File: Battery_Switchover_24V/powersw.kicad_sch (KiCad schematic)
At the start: 19 parts, among them Q2 NMOS, Q3 NMOS, Q4 NMOS, Q5 NMOS, Q6 NMOS, Q7 NMOS, U2 LM74610QDGKRQ1

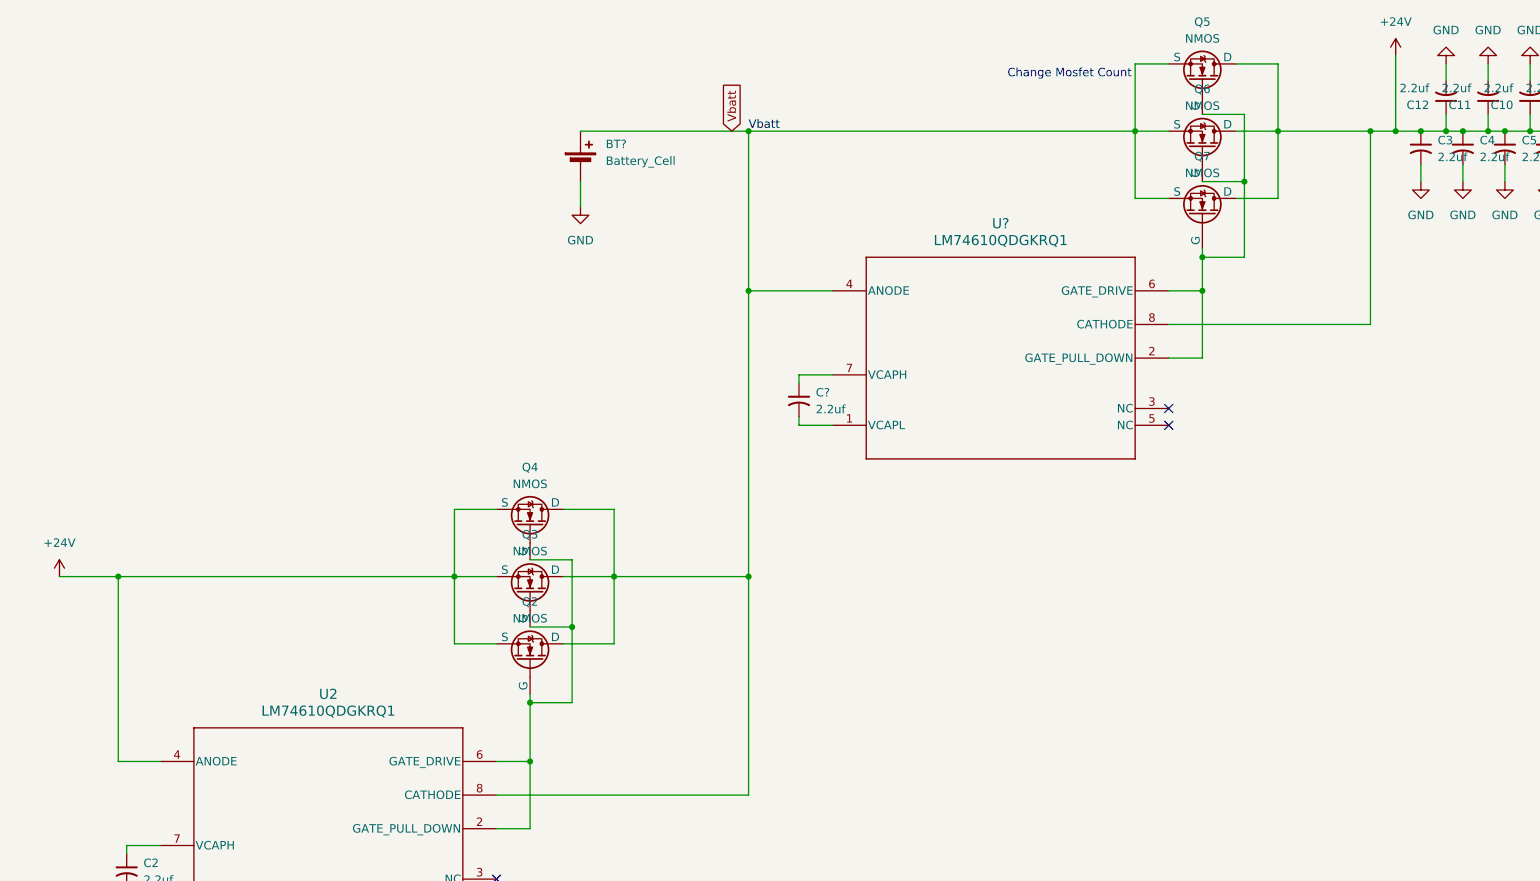
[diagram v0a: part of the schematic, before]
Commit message: General Improvements
Mosfet sayısı 1 e düştü polarize cap ler değiştirildi voltage converter değiştirildi
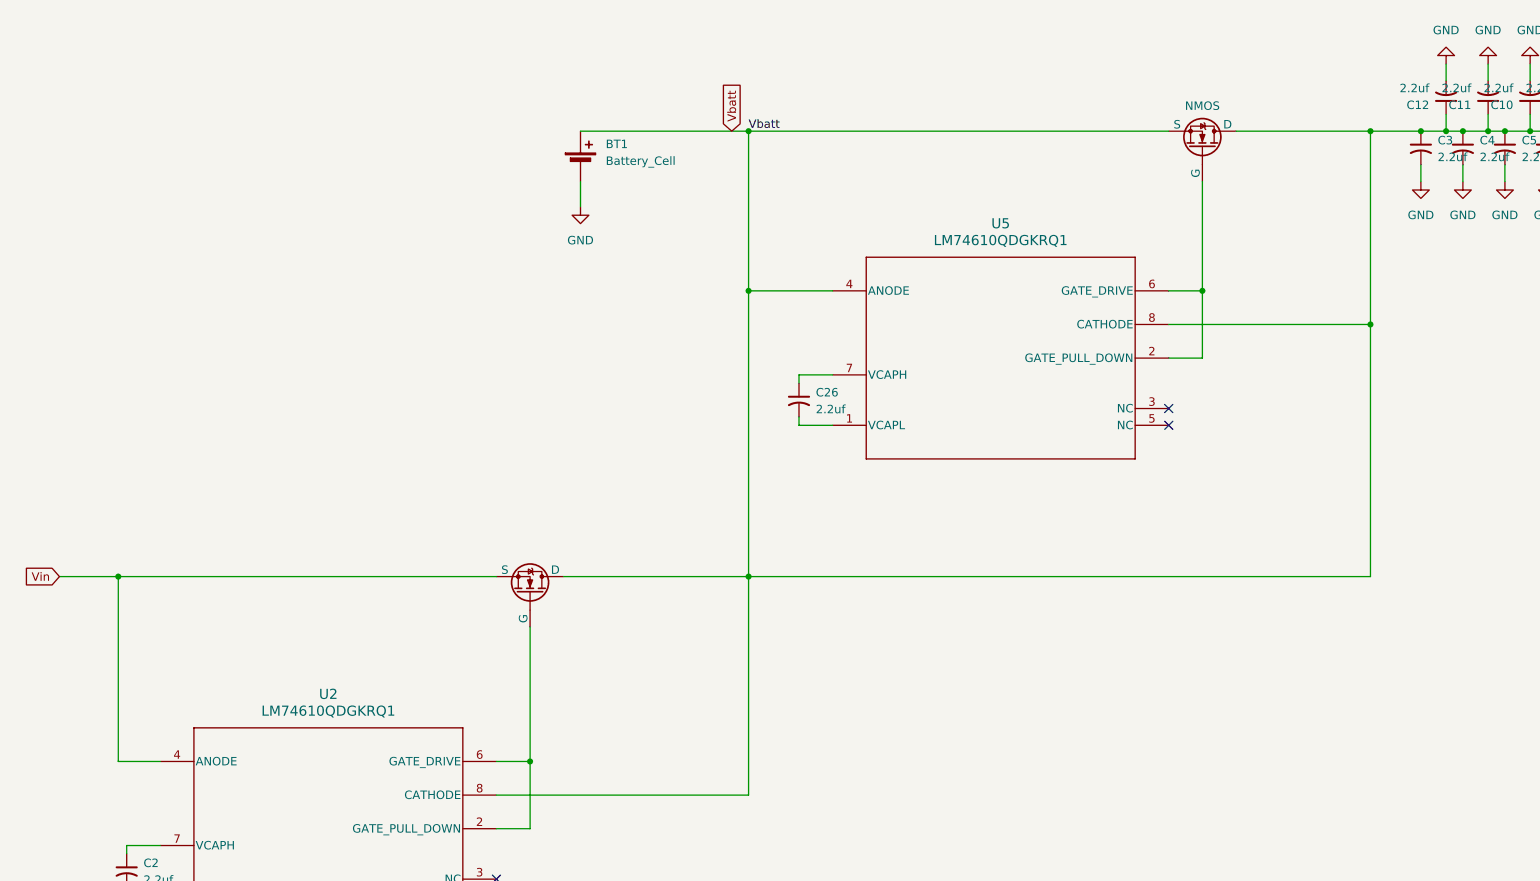
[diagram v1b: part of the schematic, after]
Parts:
- removed Q2, Q4, Q5, Q7: NMOS, symbol Simulation_SPICE:NMOS
- gave numbers to parts that had none: 3
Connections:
- net Vbatt: now also C10.1, C11.1, C12.1, C3.1, C4.1, C5.1, C6.1, C9.1, Q6.1 (D), U5.8 (CATHODE)
- removed net +24V: C10.1, C11.1, C12.1, C3.1, C4.1, C5.1, C6.1, C9.1, Q3.3 (S), Q6.1 (D), U2.4 (ANODE), U5.8 (CATHODE)
- new net Vin: Q3.3 (S), U2.4 (ANODE)
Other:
- note removed: "Change Mosfet Count"

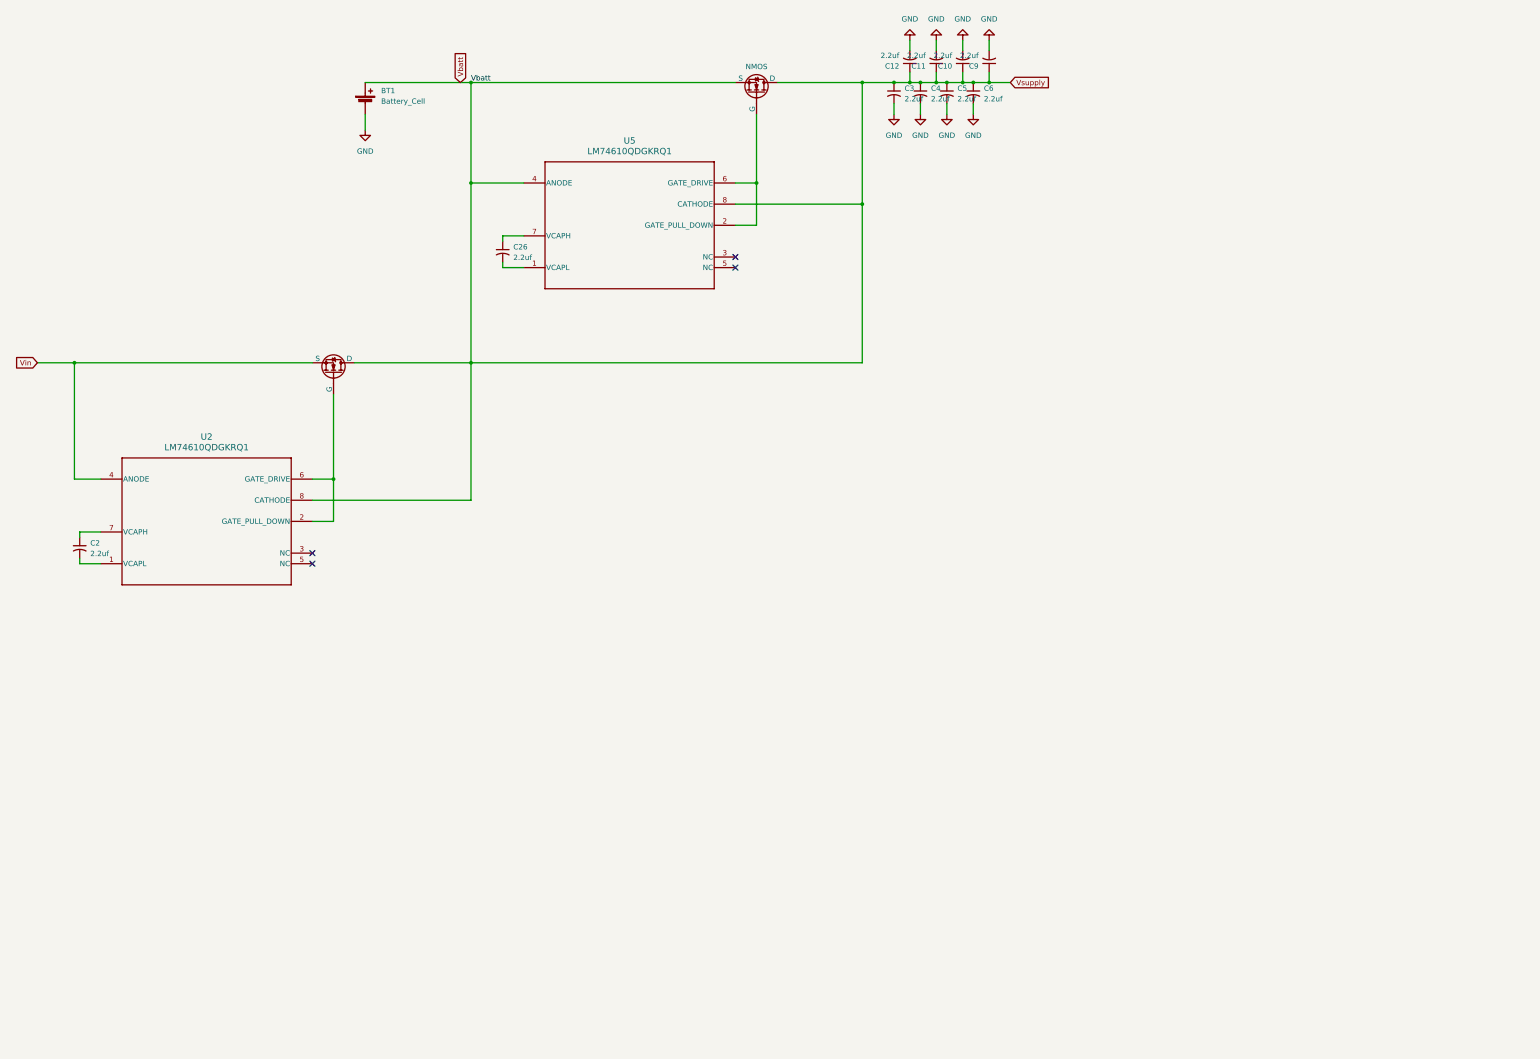
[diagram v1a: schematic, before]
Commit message: Isı kontrollü eklendi bazı parçaların sembolleri değişti
Mosfetlere doğru semboller eklendi Isı kontorll IC eklendi Ledlerin bağlantıları yapıldı
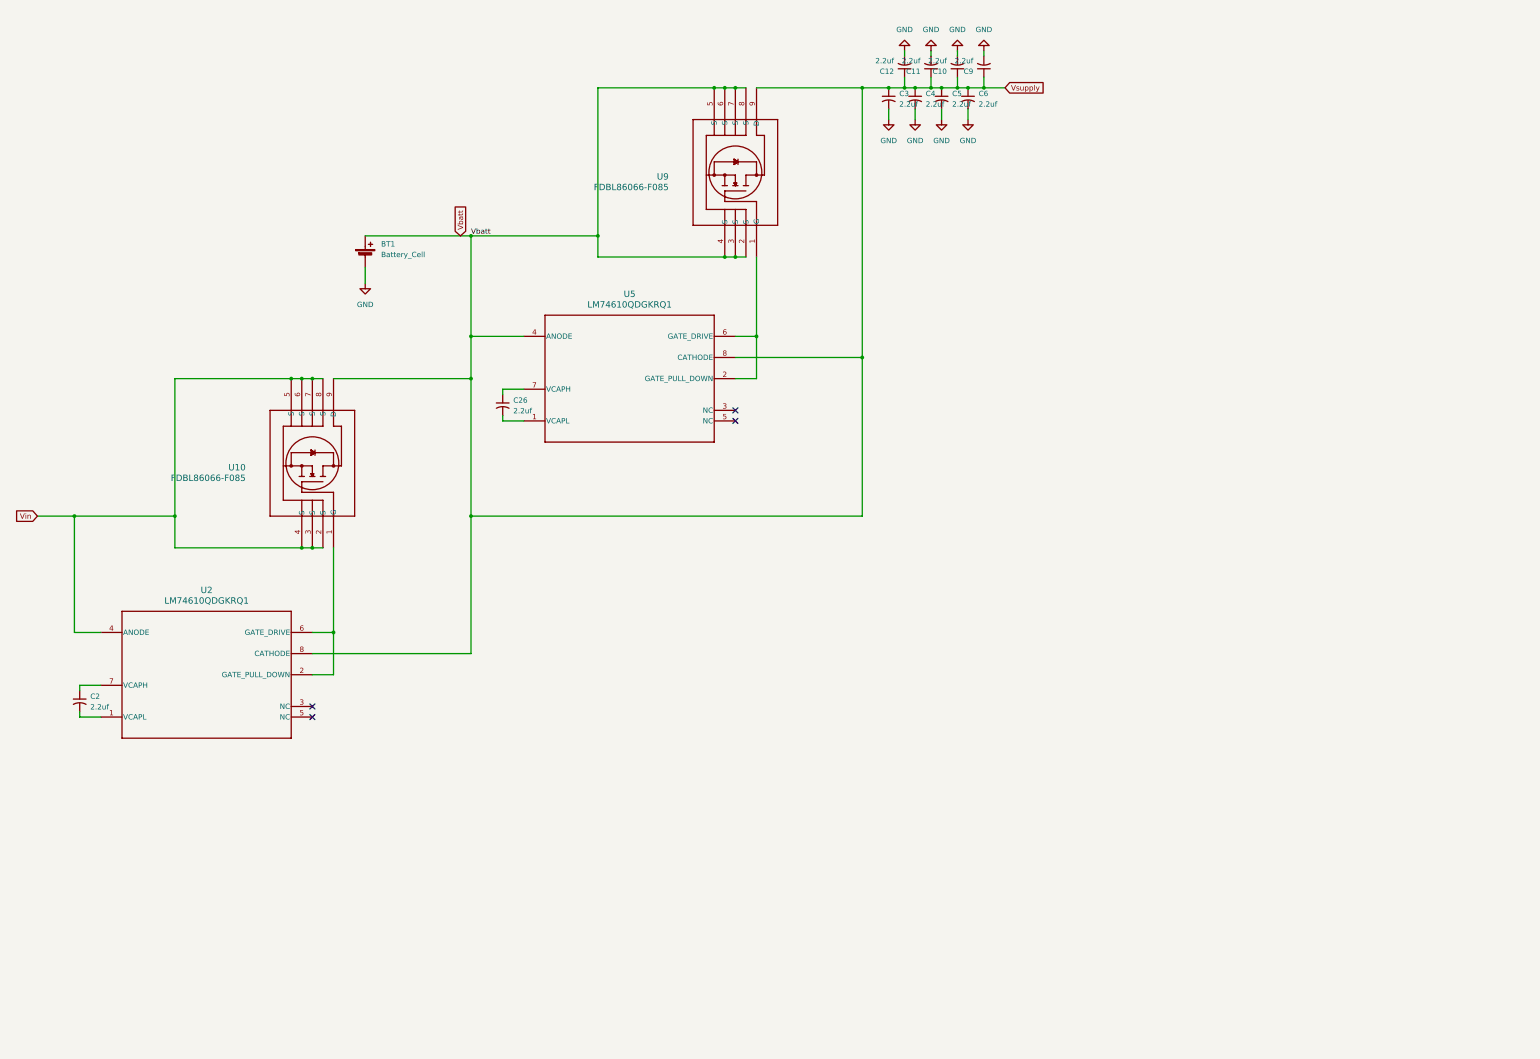
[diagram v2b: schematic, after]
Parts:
- removed Q3, Q6: NMOS, symbol Simulation_SPICE:NMOS
- added U10, U9: FDBL86066-F085, H-PSOF8L_ONS, symbol FDBL86062:FDBL86066-F085
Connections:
- net Vbatt: now also U10.9 (D), U9.2 (S), U9.3 (S), U9.4 (S), U9.5 (S), U9.6 (S), U9.7 (S), U9.8 (S), U9.9 (D)
- net Vin: now also U10.2 (S), U10.3 (S), U10.4 (S), U10.5 (S), U10.6 (S), U10.7 (S), U10.8 (S)
- net at U5.2 (GATE_PULL_DOWN), U5.6 (GATE_DRIVE): now also U9.1 (G)
- net at U2.2 (GATE_PULL_DOWN), U2.6 (GATE_DRIVE): now also U10.1 (G)
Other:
- moved on the sheet: BT1, C10, C11, C12, C2, C26, C3, C4, C5, C6, C9, U2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

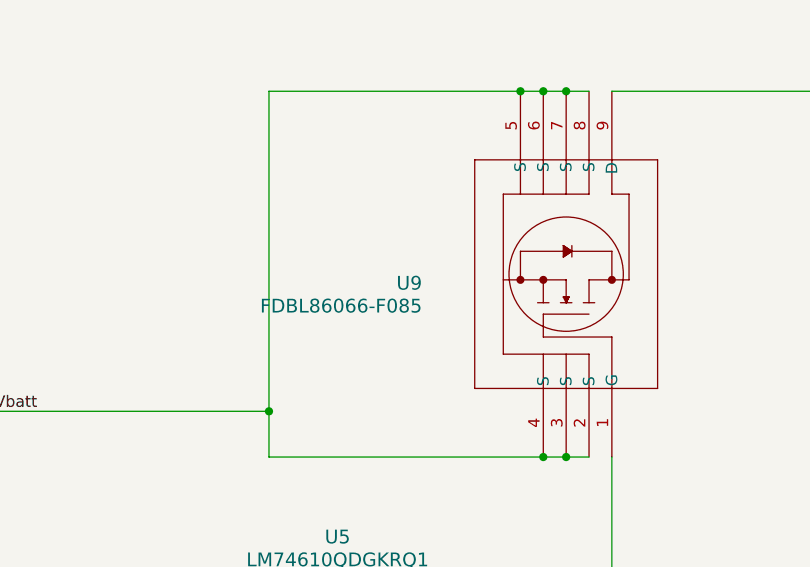
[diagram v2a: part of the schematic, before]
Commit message: Added SCL and SDA from the tempreture sensor to the CPU
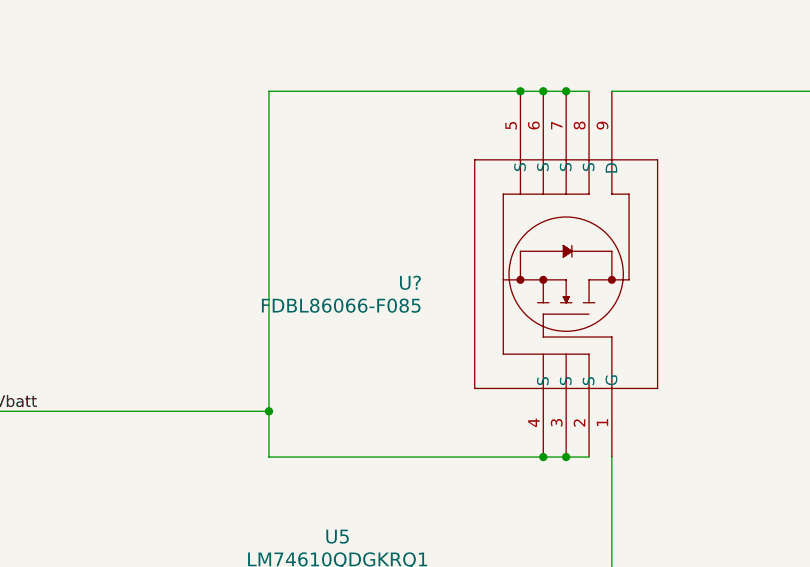
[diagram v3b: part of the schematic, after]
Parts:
- renumbered U9 to U?
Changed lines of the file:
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@@
 		(on_board yes)
 		(dnp no)
-		(property "Reference" "U9"
+		(property "Reference" "U?"
 			(at 175.768 55.626 90)
 			(effects
@@
 		(pin "1"
 		)
+		(instances
+			(project "Battery_Switchover_24V"
+				(path "/045845e0-5d00-4da8-961e-99bdf190f683/40a8593a-1917-4d96-a386-ebab07cd1c69"
+					(reference "U?")
+					(unit 1)
+				)
+			)
+		)
 	)

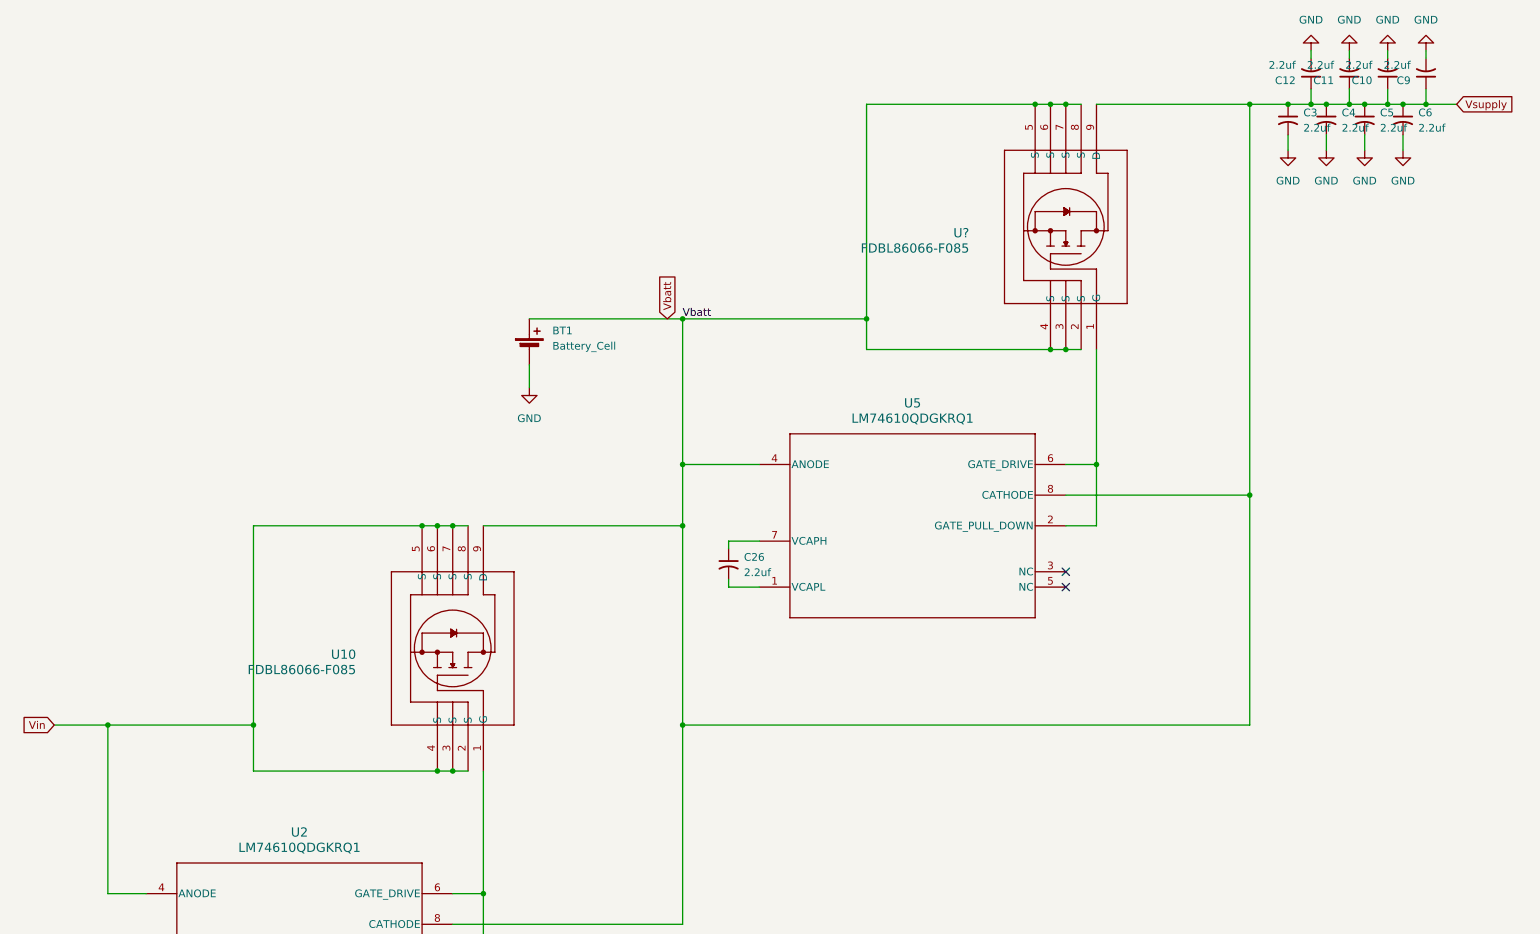
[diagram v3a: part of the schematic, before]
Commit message: Added Some Protection MEasures and redid the Fan Contrlll
Added TVS diodes battery monitor inputs and outputs and some capacitors added fan controll fixed output capacitances of battery monitoring circuit
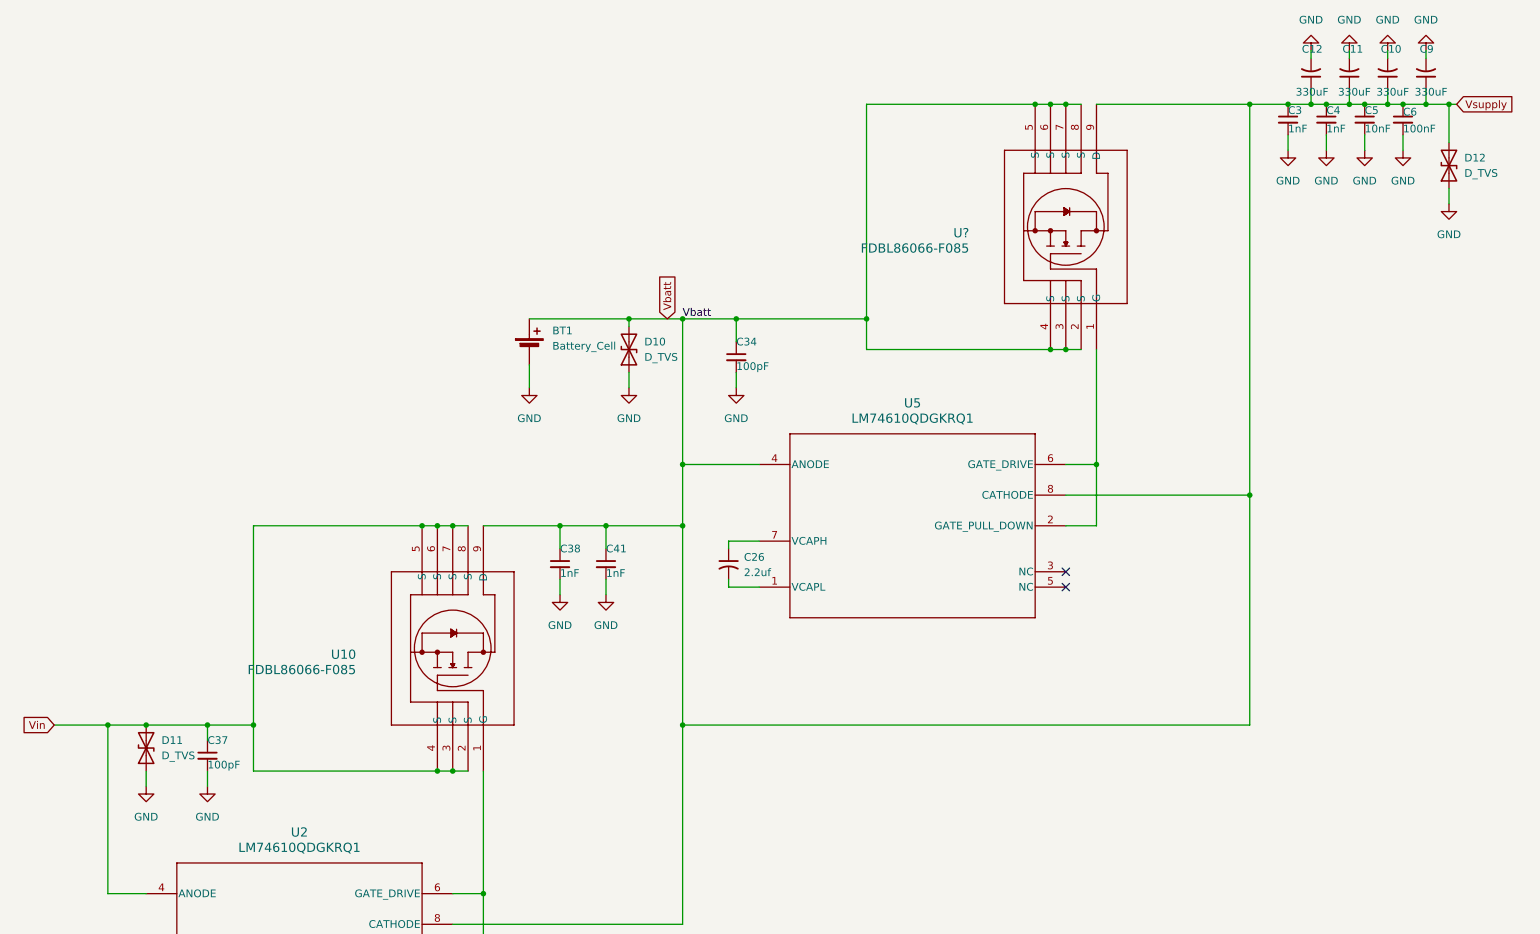
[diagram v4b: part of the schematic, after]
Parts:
- removed C3, C4, C5, C6: 2.2uf, symbol Device:C_Small_US
- added C3, C38, C4, C41: 1nF, symbol Device:C_Small
- added C34, C37: 100pF, symbol Device:C_Small
- added C5: 10nF, symbol Device:C_Small
- added C6: 100nF, symbol Device:C_Small
- added D10, D11, D12: D_TVS, symbol Device:D_TVS
- C10, C11, C12, C9: value 2.2uf -> 330uF
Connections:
- net GND: now also C3.2, C34.2, C37.2, C38.2, C4.2, C41.2, C5.2, C6.2, D10.1 (A1), D11.1 (A1), D12.1 (A1)
- net Vbatt: now also C3.1, C34.1, C38.1, C4.1, C41.1, C5.1, C6.1, D10.2 (A2), D12.2 (A2)
- net Vin: now also C37.1, D11.2 (A2)
